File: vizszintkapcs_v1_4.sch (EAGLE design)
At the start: 91 parts, among them IC2 7815TV, J10 PWR, J3 PWR, Q2 32.768kHz, Q4 CSTCR4M00G15L99, U1 MCP3004-I/ST, U6 MSP430F5529IPNR

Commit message: without MCU
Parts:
- removed C15, C16: 220n, rcl:C-EUCM0402
- removed C17: 1n, rcl:C-EUCM0402
- removed C18: 470n, rcl:C-EUCM0402
- removed C19, C20, C21, C29: 100n, rcl:C-EUCM0402
- removed C23, C24: 10p, rcl:C-EUCM0402
- removed C25, C26: 12p, rcl:C-EUCM0402
- removed C27: 4u7, rcl:CPOL-EUA/3216-18R
- removed C30: 10u, rcl:CPOL-EUA/3216-18R
- removed H1, H2: MOUNT-PAD-SQUARE4.1, holes:MOUNT-PAD-SQUARE4.1
- removed J10, J3: PWR, pinhead:PINHD-1X3
- removed JP1: +5V, jumper:JP1M
- removed JP10, JP12, JP5, JP6, JP7, JP9: (no value), SparkFun:JUMPER-2PTH
- removed JP11: USB-A-H, SparkFun-Connectors:USB-A-H
- removed JP2: +3V3, jumper:JP1M
- removed JP3: GND, jumper:JP1M
- removed JP4: (no value), pinhead-1:PINHD-1X2_2.00
- removed JP4.1: SBW_TST, jumper:JP1M
- removed JP4.2: SBW_RST, jumper:JP1M
- removed JP4.3: SBW_NC, jumper:JP1M
- removed JP6.1: TXD, jumper:JP1M
- removed JP6.2: RXD, jumper:JP1M
- removed JP6.3: CTS, jumper:JP1M
- removed JP6.4: RTS, jumper:JP1M
- removed JP8: LED1_PWR, jumper:JP1E
- removed LD1117: V_REG_LD1117VXX, SparkFun-PowerIC:V_REG_LD1117VXX
- removed LED1, LED2: (no value), led:LEDCHIPLED_0603
- removed LSP1, LSP10, LSP2, LSP3, LSP4, LSP5, LSP6, LSP7, LSP8, LSP9, WATERIN: SE14, solpad:SE14
- removed NRF24_MODULE: M04X2, SparkFun-Connectors:M04X2
- removed Q2: 32.768kHz, microcrystal:MS3V-T1R
- removed Q4: CSTCR4M00G15L99, murata:MURATA-FILTER_CSTCR6M00G53Z
- removed R14: 100R, rcl:R-EU_RM0402
- removed R15: 1k4, rcl:R-EU_RM0402
- removed R16: 1M, rcl:R-EU_RM0402
- removed R27: 47k, rcl:R-EU_RM0402
- removed R28: 0R, rcl:R-EU_RM0402
- removed R29, R30: 470R, rcl:R-EU_RM0402
- removed R31, R32: 27R, rcl:R-EU_RM0402
- removed S1, S2: (no value), electricalmeter:PB
- removed S3: RST, electricalmeter:PB
- removed S4: (no value), adafruit:EG1218S
- removed S5: BSL, electricalmeter:PB
- removed U6: MSP430F5529IPNR, TI_MSP430_v16_intern:F552X---PN80
- added IC1: UA78M08DCY, linear:UA78M08DCY
- added U$2: STMICRO_L7808, forCNC:STMICRO_L7808
- added U$3: TERMINAL_BLOCK_4:METZ_AST1350404, forCNC:TERMINAL_BLOCK_4:METZ_AST1350404
- added U$6: TERMINAL_BLOCK_6:METZ_AST1350604, forCNC:TERMINAL_BLOCK_6:METZ_AST1350604
- added U$8: TERMINAL_BLOCK_10:METZ_AST0451004, forCNC:TERMINAL_BLOCK_10:METZ_AST0451004
- 7805: value (none) -> FAIRCHILD_LM7805CT; device SparkFun-PowerIC:V_REG_78XXSINK -> forCNC:FAIRCHILD_LM7805CT
- C5: value 100n -> 470uF; device rcl:C-EUCM0402 -> capacitor-wima:C2,5-3
- C6: value 10uF -> 10nF
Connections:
- removed net +3V3: C19.2, C20.1, C30.+, C5.1, J10.3, JP2.2, R27.2, R28.2, S5.P, U6.18, U6.50
- removed net +5V: C21.1, C27.+, J3.3, JP1.2, U6.65
- removed net 7805_DC5V: 7805.OUT, C3.1, C9.1, S4.S
- removed net AVCC: C29.1, R28.1, U6.11
- removed net CE_NRF: JP12.2, NRF24_MODULE.3
- removed net CSN_NRF: JP7.1, NRF24_MODULE.4
- removed net EZFET_SBW_NC: JP4.3.1
- removed net EZFET_SBW_RST: JP4.2.1
- removed net EZFET_SBW_TST: JP4.1.1
- removed net EZFET_UARTCTS: JP6.4.1
- removed net EZFET_UARTRTS: JP6.3.1
- removed net EZFET_UARTRXD: JP6.1.1
- removed net EZFET_UARTTXD: JP6.2.1
- removed net HUB_DM1: JP4.1, R31.1
- removed net HUB_DP1: JP4.2, R32.1
- removed net IRQ_NRF: JP6.1, NRF24_MODULE.8
- removed net MISO_NRF: JP10.2, NRF24_MODULE.7
- removed net MOSI_NRF: JP5.1, NRF24_MODULE.6
- removed net MOTOR_SENSE: C17.1
- removed net N$3: LED2.A
- removed net N$32: LED1.A, R29.2
- removed net N$35: LED2.A, R30.2
- removed net N$4: LED1.A, R14.1, S5.S
- removed net N$7: JP8.2, R29.1
- removed net P1.0: JP8.1, U6.21
- removed net P1.1: S2.P, U6.22
- removed net P1.2: JP6.2, U6.23
- removed net P1.7: JP6.3.2, U6.28
- removed net P2.0: U6.29
- removed net P2.1: S1.P, U6.30
- removed net P2.2: U6.31
- removed net P2.3: JP12.1, U6.32
- removed net P2.6: U6.35
- removed net P3.0: JP5.2, U6.37
- removed net P3.1: JP10.1, U6.38
- removed net P3.2: JP9.1, U6.39
- removed net P3.3: U6.40
- removed net P3.4: U6.41
- removed net P3.5: U6.42
- removed net P3.6: U6.43
- removed net P3.7: U6.44
- removed net P4.0: U6.45
- removed net P4.1: U6.46
- removed net P4.2: U6.47
- removed net P4.4/UCA1TXD: JP6.1.2, U6.51
- removed net P4.5/UCA1RXD: JP6.2.2, U6.52
- removed net P4.7: R30.1, U6.54
- removed net P5.2/XT2IN: Q4.3, U6.69
- removed net P5.3/XT2OUT: Q4.1, U6.70
- removed net P5.4/XIN: C26.2, Q2.2, U6.12
- removed net P5.5/XOUT: C25.2, Q2.1, U6.13
- removed net P6.2: U6.79
- removed net P6.3: U6.80
- removed net P6.4: U6.1
- removed net P6.5: U6.2
- removed net P6.6: U6.3
- removed net P6.7: JP6.4.2, U6.4
- removed net P7.0: U6.5
- removed net P7.4: U6.57
- removed net P8.1: U6.16
- removed net P8.2: U6.17
- removed net RST/SBWTDIO: C17.1, JP4.2.2, R27.1, S3.S, U6.76
- removed net SCK_NRF: JP9.2, NRF24_MODULE.5
- removed net TARGET_DM: C24.1, R31.2, U6.64
- removed net TARGET_DP: C23.1, R15.2, R32.2, U6.62
- removed net TARGET_PUR: R14.2, R15.1, R16.2, U6.63
- removed net TARGET_VUSB: C16.1, U6.66
- removed net TEST/SBWTCK: JP4.1.2, U6.71
- removed net USB_5V: JP11.VBUS, S4.O
- removed net V18: C15.1, U6.67
- removed net VCORE: C18.2, U6.20
- new net COMMON_EARTH: U$8.P$10, U$8.P$2, U$8.P$5, U$8.P$8
- new net DC8V: C5.1, C6.1, U$2.OUT, U$3.P$4
- new net MOTOR_OUT: C1.1, U$1.IP-@3, U$1.IP-@4
- net 1_WATER_IN: now also U$6.P$1; no longer LSP5.MP
- net 230V0: now also U$8.P$3; no longer H2.MOUNT
- net 230VPHASE: now also U$8.P$1; no longer H1.MOUNT
- net 2_WATER_IN: now also U$6.P$2; no longer LSP6.MP
- net 3V3FTDI: no longer JP2.1
- net 3_WATER_IN: now also U$6.P$3; no longer LSP7.MP
- net 4_WATER_IN: now also U$6.P$4; no longer LSP8.MP
- net 5_WATER_IN: now also U$6.P$5; no longer LSP9.MP
- net 6_WATER_IN: now also U$6.P$6; no longer LSP10.MP
- net AC12V: now also U$3.P$2; no longer WATERIN.MP
- net D+: no longer JP11.D+
- net D-: no longer JP11.D-
- net DC3.3V: now also IC1.VO; no longer C6.2, JP2.1, LD1117.OUT, NRF24_MODULE.2
- net DC5V: now also 7805.OUT, C3.1, C9.1; no longer C16.1, JP1.1, LD1117.IN, S4.P
- net GND: now also C6.2, IC1.GND, IC1.GND@1, U$2.GND, U$3.P$3; no longer C15.2, C16.2, C17.2, C18.1, C19.1, C20.2, C21.2, C23.2, C24.2, C25.1, C26.1, C27.-, C29.2, C30.-, C6.1, J10.1, J10.2, J3.1, J3.2, JP11.GND, JP3.1, JP3.2, LD1117.GND, LED1.C, LED2.C, NRF24_MODULE.1, Q2.GND, Q4.2, R16.1, S1.S, S2.S, S3.P, U6.14, U6.19, U6.49, U6.61, U6.68
- net MOTOR_DIRECT_1: now also U1.CH0; no longer U1.CH2
- net MOTOR_DIRECT_2: now also U1.CH2; no longer U1.CH3
- net MOTOR_IN: now also U$8.P$4; no longer C1.1, LSP1.MP, U$1.IP-@3, U$1.IP-@4
- net MOTOR_IN_2: now also U$8.P$7; no longer LSP3.MP
- net MOTOR_OUT_1: now also U$8.P$6; no longer LSP2.MP
- net MOTOR_OUT_2: now also U$8.P$9; no longer LSP4.MP
- net N$1: no longer LED1.C
- net N$2: no longer LED2.C
- net N$26: no longer C15.1
- net P1.3: no longer U6.24
- net P1.4: no longer U6.25
- net P1.5: no longer U6.26
- net P1.6: no longer U6.27
- net P2.4: no longer JP7.2, U6.33
- net P2.5: no longer U6.34
- net P2.7: no longer U6.36
- net P4.3: no longer U6.48
- net P6.0: now also U1.CH3; no longer U1.CH1, U6.77
- net P6.1: now also U1.CH1; no longer U1.CH0, U6.78
- net REC12V: now also IC1.VI
- net REC24V: now also U$2.IN
- net VCC: no longer JP2.3
- net VCCIO: no longer JP2.2
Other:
- note removed: "1.6"
- note removed: "<<"
- note removed: "Analog VCC"
- note removed: "BSL"
- note removed: "Connections"
- note removed: "Design Notes:"
- note removed: "Free IO pins: 4.6, 5.0, 5.1, 5.6, 5.7, 7.1, 7.2, 7.3, 7.5, 7.6, 7.7, 8.0, PJ.x (4)"
- note removed: "LFXTCLK"
- note removed: "Main MSP430F5529 w Power, Clock and USB"
- note removed: "RESET"
- note removed: "Remove R28 and inject AVCC directly if needed"
- note removed: "Speed"
- note removed: "User Buttons"
- note removed: "User LEDs"
- note removed: "XT2"
- note removed: "ezFET <<---->> LaunchPad"
- moved on the sheet: C5, C6

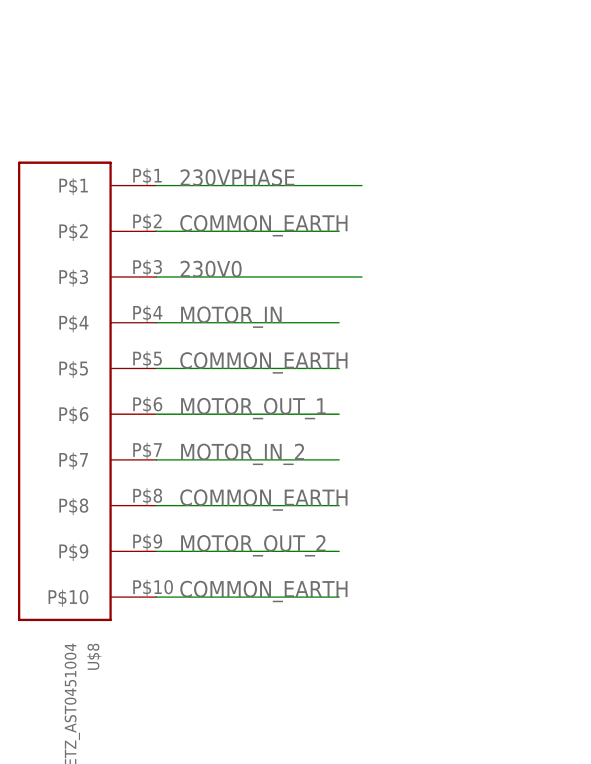
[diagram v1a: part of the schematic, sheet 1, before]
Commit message: smaller version with danger sign and good holes
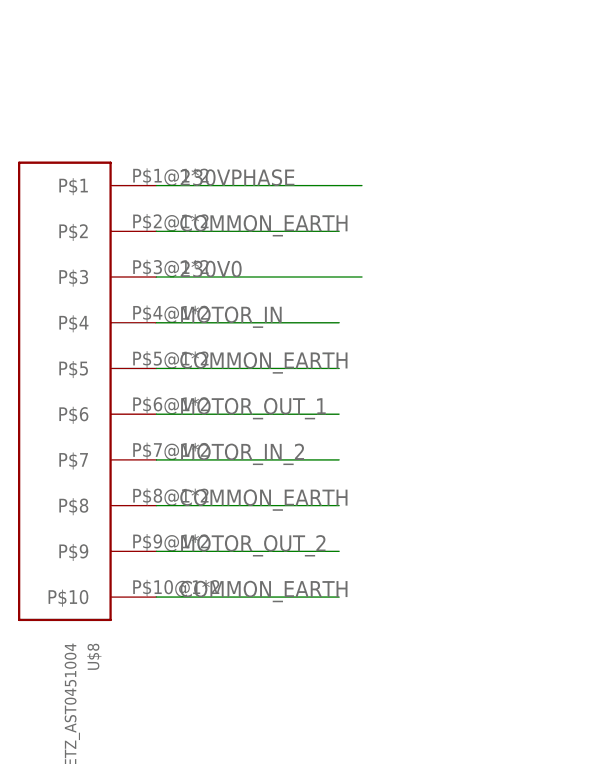
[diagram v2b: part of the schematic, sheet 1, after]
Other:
- moved on the sheet: U$8

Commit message: save
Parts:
- B2, B7: device rectifier:RB1A -> rectifier:1KAB
- C1, C10, C13, C2, C3, C5: device capacitor-wima:C2,5-3 -> adafruit:CPOL-USE3.5-8
- IC1: value UA78M08DCY -> UA78M33DCY; device linear:UA78M08DCY -> linear:UA78M33DCY
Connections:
- net DC15V: now also C13.+; no longer C13.1
- net DC3.3V: now also C1.+; no longer C1.1
- net DC5V: now also C3.+; no longer C3.1
- net DC8V: now also C5.+; no longer C5.1
- net GND: now also C1.-, C10.-, C13.-, C2.-, C5.-; no longer C10.2, C13.2, C2.2, C3.2, C5.2
- net REC12V: now also C2.+; no longer C2.1
- net REC24V: now also C10.+; no longer C10.1
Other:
- note added: "NEM FELTÉTLEN KELL 5->3 DE A BUFFER HASZNOS"
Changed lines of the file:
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@@
 <part name="GND4" library="SparkFun-Aesthetics" deviceset="GND" device=""/>
 <part name="GND5" library="SparkFun-Aesthetics" deviceset="GND" device=""/>
-<part name="C2" library="capacitor-wima" deviceset="C" device="2,5-3" value="470uF"/>
+<part name="C2" library="adafruit" deviceset="CPOL-US" device="E3.5-8" value="470uF"/>
 <part name="7805" library="forCNC" deviceset="FAIRCHILD_LM7805CT" device=""/>
-<part name="C3" library="capacitor-wima" deviceset="C" device="2,5-3" value="470uF"/>
+<part name="C3" library="adafruit" deviceset="CPOL-US" device="E3.5-8" value="470uF"/>
 <part name="GND6" library="SparkFun-Aesthetics" deviceset="GND" device=""/>
 <part name="GND7" library="SparkFun-Aesthetics" deviceset="GND" device=""/>
 <part name="C7" library="SparkFun-Capacitors" deviceset="CAP" device="1206" value="10NF"/>
 <part name="C9" library="SparkFun-Capacitors" deviceset="CAP" device="1206" value="10nF"/>
-<part name="B7" library="rectifier" deviceset="RB1A" device=""/>
+<part name="B7" library="rectifier" deviceset="1KAB" device=""/>
 <part name="GND2" library="SparkFun-Aesthetics" deviceset="GND" device=""/>
 <part name="GND9" library="SparkFun-Aesthetics" deviceset="GND" device=""/>
-<part name="C10" library="capacitor-wima" deviceset="C" device="2,5-3" value="470uF"/>
+<part name="C10" library="adafruit" deviceset="CPOL-US" device="E3.5-8" value="470uF"/>
 <part name="C12" library="SparkFun-Capacitors" deviceset="CAP" device="1206" value="10NF"/>
-<part name="B2" library="rectifier" deviceset="RB1A" device=""/>
+<part name="B2" library="rectifier" deviceset="1KAB" device=""/>
 <part name="IC2" library="linear" deviceset="78*" device="TV" technology="15"/>
-<part name="C13" library="capacitor-wima" deviceset="C" device="2,5-3" value="470uF"/>
+<part name="C13" library="adafruit" deviceset="CPOL-US" device="E3.5-8" value="470uF"/>
 <part name="GND11" library="SparkFun-Aesthetics" deviceset="GND" device=""/>
 <part name="GND13" library="SparkFun-Aesthetics" deviceset="GND" device=""/>
@@
 <part name="GND1" library="SparkFun-Aesthetics" deviceset="GND" device=""/>
 <part name="GND3" library="SparkFun-Aesthetics" deviceset="GND" device=""/>
-<part name="C1" library="capacitor-wima" deviceset="C" device="2,5-3" value="470uF"/>
+<part name="C1" library="adafruit" deviceset="CPOL-US" device="E3.5-8" value="470uF"/>
 <part name="C4" library="SparkFun-Capacitors" deviceset="CAP" device="1206" value="10nF"/>
 <part name="U1" library="Microchip_By_element14_Batch_1" deviceset="MCP3004-I/ST" device=""/>
@@
 <part name="GPIO_CON1" library="con-harting-ml" deviceset="ML40" device="R" value="BH40R"/>
 <part name="U$2" library="forCNC" deviceset="STMICRO_L7808" device=""/>
-<part name="C5" library="capacitor-wima" deviceset="C" device="2,5-3" value="470uF"/>
+<part name="C5" library="adafruit" deviceset="CPOL-US" device="E3.5-8" value="470uF"/>
 <part name="C6" library="SparkFun-Capacitors" deviceset="CAP" device="1206" value="10nF"/>
 <part name="U$6" library="forCNC" deviceset="TERMINAL_BLOCK_6:METZ_AST1350604" device=""/>
 <part name="U$8" library="forCNC" deviceset="TERMINAL_BLOCK_10:METZ_AST0451004" device=""/>
 <part name="U$3" library="forCNC" deviceset="TERMINAL_BLOCK_4:METZ_AST1350404" device=""/>
-<part name="IC1" library="linear" deviceset="UA78M*" device="DCY" technology="08"/>
+<part name="IC1" library="linear" deviceset="UA78M*" device="DCY" technology="33" value="UA78M33DCY"/>
 </parts>
 <sheets>
@@
 2.4
 2.5</text>
+<text x="424.18" y="124.46" size="1.778" layer="91">NEM FELTÉTLEN KELL 5-&gt;3 DE A BUFFER HASZNOS</text>
 </plain>
 <moduleinsts>
@@
 </segment>
 <segment>
-<pinref part="C2" gate="G$1" pin="2"/>
+<pinref part="C2" gate="G$1" pin="-"/>
 <pinref part="GND5" gate="1" pin="GND"/>
 <wire x1="127" y1="7.62" x2="127" y2="5.08" width="0.1524" layer="91"/>
@@
 </segment>
 <segment>
-<pinref part="C3" gate="G$1" pin="2"/>
+<pinref part="C3" gate="G$1" pin="-"/>
 <pinref part="GND7" gate="1" pin="GND"/>
 <wire x1="193.04" y1="5.08" x2="193.04" y2="7.62" width="0.1524" layer="91"/>
@@
 </segment>
 <segment>
-<pinref part="C10" gate="G$1" pin="2"/>
+<pinref part="C10" gate="G$1" pin="-"/>
 <pinref part="GND9" gate="1" pin="GND"/>
 <wire x1="127" y1="-33.02" x2="127" y2="-35.56" width="0.1524" layer="91"/>
@@
 </segment>
 <segment>
-<pinref part="C13" gate="G$1" pin="2"/>
+<pinref part="C13" gate="G$1" pin="-"/>
 <pinref part="GND13" gate="1" pin="GND"/>
 <wire x1="177.8" y1="-35.56" x2="177.8" y2="-33.02" width="0.1524" layer="91"/>
@@
 <pinref part="GND3" gate="1" pin="GND"/>
 <wire x1="208.28" y1="25.4" x2="198.12" y2="25.4" width="0.1524" layer="91"/>
-<pinref part="C1" gate="G$1" pin="2"/>
+<pinref part="C1" gate="G$1" pin="-"/>
 <wire x1="198.12" y1="27.94" x2="198.12" y2="25.4" width="0.1524" layer="91"/>
 </segment>
@@
 <wire x1="165.1" y1="-66.04" x2="165.1" y2="-73.66" width="0.1524" layer="91"/>
 <label x="165.1" y="-73.66" size="1.778" layer="95" rot="R90"/>
-<pinref part="C5" gate="G$1" pin="2"/>
+<pinref part="C5" gate="G$1" pin="-"/>
 <wire x1="165.1" y1="-73.66" x2="165.1" y2="-76.2" width="0.1524" layer="91"/>
 <wire x1="182.88" y1="-63.5" x2="182.88" y2="-73.66" width="0.1524" layer="91"/>
@@
 <segment>
 <wire x1="104.14" y1="17.78" x2="119.38" y2="17.78" width="0.1524" layer="91"/>
-<pinref part="C2" gate="G$1" pin="1"/>
+<pinref part="C2" gate="G$1" pin="+"/>
 <wire x1="119.38" y1="17.78" x2="127" y2="17.78" width="0.1524" layer="91"/>
 <wire x1="127" y1="17.78" x2="127" y2="15.24" width="0.1524" layer="91"/>
@@
 </segment>
 <segment>
-<pinref part="C3" gate="G$1" pin="1"/>
+<pinref part="C3" gate="G$1" pin="+"/>
 <wire x1="193.04" y1="17.78" x2="203.2" y2="17.78" width="0.1524" layer="91"/>
 <wire x1="193.04" y1="15.24" x2="193.04" y2="17.78" width="0.1524" layer="91"/>
@@
 <segment>
 <wire x1="104.14" y1="-22.86" x2="119.38" y2="-22.86" width="0.1524" layer="91"/>
-<pinref part="C10" gate="G$1" pin="1"/>
+<pinref part="C10" gate="G$1" pin="+"/>
 <wire x1="119.38" y1="-22.86" x2="127" y2="-22.86" width="0.1524" layer="91"/>
 <wire x1="127" y1="-22.86" x2="127" y2="-25.4" width="0.1524" layer="91"/>
@@
 <segment>
 <wire x1="177.8" y1="-22.86" x2="187.96" y2="-22.86" width="0.1524" layer="91"/>
-<pinref part="C13" gate="G$1" pin="1"/>
+<pinref part="C13" gate="G$1" pin="+"/>
 <wire x1="187.96" y1="-22.86" x2="195.58" y2="-22.86" width="0.1524" layer="91"/>
 <wire x1="177.8" y1="-25.4" x2="177.8" y2="-22.86" width="0.1524" layer="91"/>
@@
 <segment>
 <wire x1="185.42" y1="38.1" x2="198.12" y2="38.1" width="0.1524" layer="91"/>
-<pinref part="C1" gate="G$1" pin="1"/>
+<pinref part="C1" gate="G$1" pin="+"/>
 <wire x1="198.12" y1="38.1" x2="198.12" y2="35.56" width="0.1524" layer="91"/>
 <wire x1="198.12" y1="38.1" x2="208.28" y2="38.1" width="0.1524" layer="91"/>
@@
 <wire x1="177.8" y1="-55.88" x2="182.88" y2="-55.88" width="0.1524" layer="91"/>
 <label x="185.42" y="-55.88" size="1.778" layer="95"/>
-<pinref part="C5" gate="G$1" pin="1"/>
+<pinref part="C5" gate="G$1" pin="+"/>
 <wire x1="182.88" y1="-55.88" x2="193.04" y2="-55.88" width="0.1524" layer="91"/>
 <junction x="182.88" y="-55.88"/>

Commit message: only 4 water level sensor on one board
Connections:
- removed net 3_WATER_IN: U$6.P$3
- removed net 6_WATER_IN: U$6.P$6
- net AC12V: now also U$6.P$3, U$6.P$6
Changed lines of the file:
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@@
 <moduleinst name="WL1" module="WATER_LEVEL_SENSOR" x="337.82" y="104.14"/>
 <moduleinst name="REL_MOT" module="RELAY_MOTOR_CONTROL" x="345.44" y="129.54"/>
-<moduleinst name="WL3" module="WATER_LEVEL_SENSOR" x="337.82" y="53.34"/>
 <moduleinst name="WL4" module="WATER_LEVEL_SENSOR" x="337.82" y="27.94"/>
 <moduleinst name="WL5" module="WATER_LEVEL_SENSOR" x="337.82" y="2.54"/>
-<moduleinst name="WL6" module="WATER_LEVEL_SENSOR" x="337.82" y="-22.86"/>
 <moduleinst name="WL2" module="WATER_LEVEL_SENSOR" x="337.82" y="78.74"/>
 <moduleinst name="5-&gt;3_2" module="5-3VANALOG_TRANSLATE" x="439.42" y="139.7"/>
@@
 <label x="198.12" y="-66.04" size="1.778" layer="95"/>
 </segment>
+<segment>
+<pinref part="U$6" gate="G$1" pin="P$3"/>
+<wire x1="261.62" y1="45.72" x2="271.78" y2="45.72" width="0.1524" layer="91"/>
+<label x="264.16" y="45.72" size="1.778" layer="95"/>
+</segment>
+<segment>
+<pinref part="U$6" gate="G$1" pin="P$6"/>
+<wire x1="261.62" y1="30.48" x2="271.78" y2="30.48" width="0.1524" layer="91"/>
+<label x="264.16" y="30.48" size="1.778" layer="95"/>
+</segment>
 </net>
 <net name="GND" class="0">
@@
 </segment>
 <segment>
-<wire x1="314.96" y1="60.96" x2="297.18" y2="60.96" width="0.1524" layer="91"/>
-<label x="297.18" y="60.96" size="1.778" layer="95"/>
-<portref moduleinst="WL3" port="GND"/>
-</segment>
-<segment>
 <wire x1="314.96" y1="35.56" x2="297.18" y2="35.56" width="0.1524" layer="91"/>
 <label x="297.18" y="35.56" size="1.778" layer="95"/>
@@
 <label x="297.18" y="10.16" size="1.778" layer="95"/>
 <portref moduleinst="WL5" port="GND"/>
-</segment>
-<segment>
-<wire x1="314.96" y1="-15.24" x2="297.18" y2="-15.24" width="0.1524" layer="91"/>
-<label x="297.18" y="-15.24" size="1.778" layer="95"/>
-<portref moduleinst="WL6" port="GND"/>
 </segment>
 <segment>
@@
 </segment>
 <segment>
-<wire x1="314.96" y1="48.26" x2="297.18" y2="48.26" width="0.1524" layer="91"/>
-<label x="297.18" y="48.26" size="1.778" layer="95"/>
-<portref moduleinst="WL3" port="TRANS_OUT"/>
-</segment>
-<segment>
 <wire x1="314.96" y1="22.86" x2="297.18" y2="22.86" width="0.1524" layer="91"/>
 <label x="297.18" y="22.86" size="1.778" layer="95"/>
@@
 <label x="297.18" y="-2.54" size="1.778" layer="95"/>
 <portref moduleinst="WL5" port="TRANS_OUT"/>
-</segment>
-<segment>
-<wire x1="314.96" y1="-27.94" x2="297.18" y2="-27.94" width="0.1524" layer="91"/>
-<label x="297.18" y="-27.94" size="1.778" layer="95"/>
-<portref moduleinst="WL6" port="TRANS_OUT"/>
 </segment>
 </net>
@@
 </segment>
 </net>
-<net name="3_WATER_IN" class="0">
-<segment>
-<portref moduleinst="WL3" port="WATER_IN_1"/>
-<wire x1="314.96" y1="50.8" x2="297.18" y2="50.8" width="0.1524" layer="91"/>
-<label x="297.18" y="50.8" size="1.778" layer="95"/>
-</segment>
-<segment>
-<pinref part="U$6" gate="G$1" pin="P$3"/>
-<wire x1="261.62" y1="45.72" x2="271.78" y2="45.72" width="0.1524" layer="91"/>
-<label x="264.16" y="45.72" size="1.778" layer="95"/>
-</segment>
-</net>
 <net name="4_WATER_IN" class="0">
 <segment>
@@
 <wire x1="261.62" y1="35.56" x2="271.78" y2="35.56" width="0.1524" layer="91"/>
 <label x="264.16" y="35.56" size="1.778" layer="95"/>
-</segment>
-</net>
-<net name="6_WATER_IN" class="0">
-<segment>
-<portref moduleinst="WL6" port="WATER_IN_1"/>
-<wire x1="314.96" y1="-25.4" x2="297.18" y2="-25.4" width="0.1524" layer="91"/>
-<label x="297.18" y="-25.4" size="1.778" layer="95"/>
-</segment>
-<segment>
-<pinref part="U$6" gate="G$1" pin="P$6"/>
-<wire x1="261.62" y1="30.48" x2="271.78" y2="30.48" width="0.1524" layer="91"/>
-<label x="264.16" y="30.48" size="1.778" layer="95"/>
 </segment>
 </net>
@@
 </segment>
 <segment>
-<wire x1="314.96" y1="58.42" x2="297.18" y2="58.42" width="0.1524" layer="91"/>
-<label x="297.18" y="58.42" size="1.778" layer="95"/>
-<portref moduleinst="WL3" port="VCC"/>
-</segment>
-<segment>
 <wire x1="314.96" y1="33.02" x2="297.18" y2="33.02" width="0.1524" layer="91"/>
 <label x="297.18" y="33.02" size="1.778" layer="95"/>
@@
 <portref moduleinst="WL5" port="VCC"/>
 </segment>
-<segment>
-<wire x1="314.96" y1="-17.78" x2="297.18" y2="-17.78" width="0.1524" layer="91"/>
-<label x="297.18" y="-17.78" size="1.778" layer="95"/>
-<portref moduleinst="WL6" port="VCC"/>
-</segment>
 </net>
 <net name="P1.4" class="0">
-<segment>
-<portref moduleinst="WL3" port="!WATER_LEVEL_1"/>
-<wire x1="314.96" y1="45.72" x2="297.18" y2="45.72" width="0.1524" layer="91"/>
-<label x="297.18" y="45.72" size="1.778" layer="95"/>
-</segment>
 <segment>
 <wire x1="502.92" y1="236.22" x2="502.92" y2="254" width="0.1524" layer="91"/>
@@
 <net name="P2.5" class="0">
 <segment>
-<portref moduleinst="WL6" port="!WATER_LEVEL_1"/>
-<wire x1="314.96" y1="-30.48" x2="297.18" y2="-30.48" width="0.1524" layer="91"/>
-<label x="297.18" y="-30.48" size="1.778" layer="95"/>
-</segment>
-<segment>
 <wire x1="495.3" y1="236.22" x2="495.3" y2="254" width="0.1524" layer="91"/>
